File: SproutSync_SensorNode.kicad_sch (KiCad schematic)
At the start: 0 parts

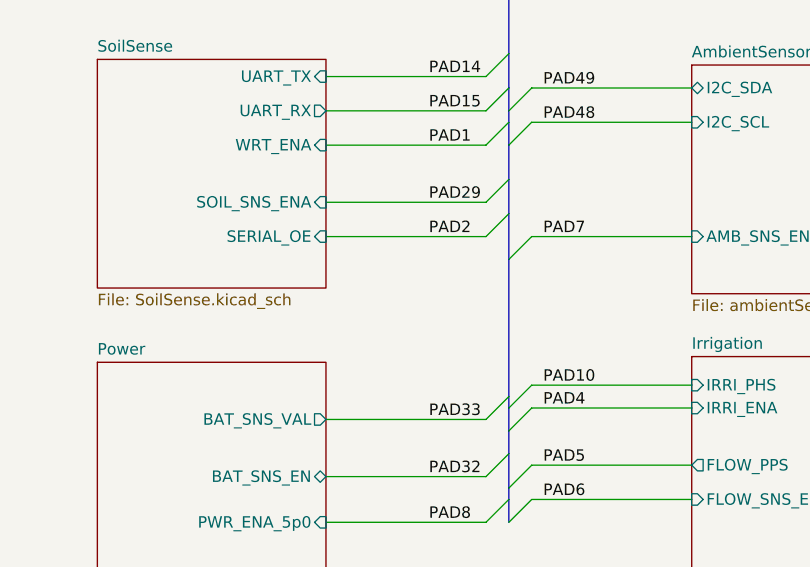
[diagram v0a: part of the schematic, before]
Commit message: replaced soil_sns frontend with SN74
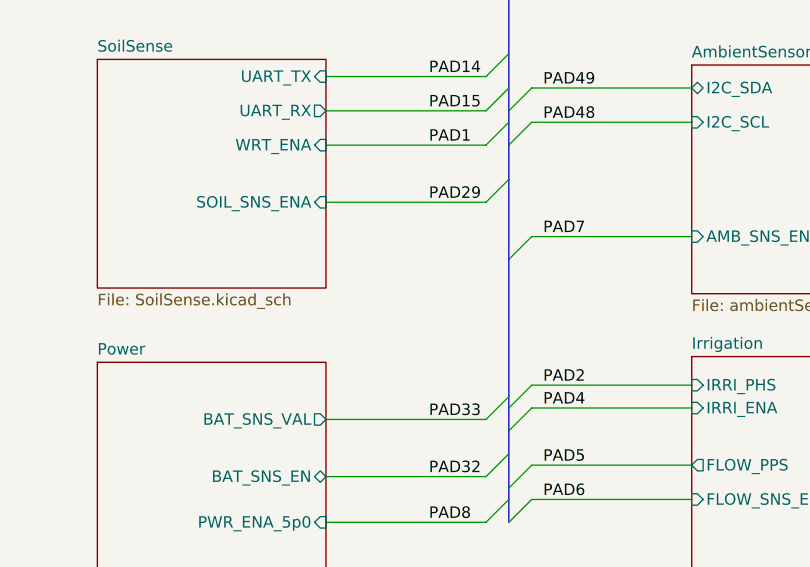
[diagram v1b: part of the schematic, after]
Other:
- sheet SoilSense ports: added none; removed SERIAL_OE
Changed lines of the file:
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@@
-	)
-	(bus_entry
-		(at 128.27 95.25)
-		(size 2.54 -2.54)
-		(stroke
-			(width 0)
-			(type default)
-		)
 	)
 	(bus_entry
@@
 		)
 	)
-	(bus
-		(pts
-			(xy 130.81 88.9) (xy 130.81 92.71)
-		)
-		(stroke
-			(width 0)
-			(type default)
-		)
-	)
 	(wire
 		(pts
@@
 	(wire
 		(pts
-			(xy 110.49 95.25) (xy 128.27 95.25)
-		)
-		(stroke
-			(width 0)
-			(type default)
-		)
-	)
-	(wire
-		(pts
 			(xy 144.78 34.29) (xy 144.78 49.53)
 		)
@@
 	(bus
 		(pts
-			(xy 130.81 92.71) (xy 130.81 97.79)
+			(xy 130.81 88.9) (xy 130.81 97.79)
 		)
 		(stroke
@@
 		)
 	)
-	(label "PAD10"
+	(label "PAD2"
 		(at 134.62 111.76 0)
-		(effects
-			(font
-				(size 1.27 1.27)
-			)
-			(justify left bottom)
-		)
-	)
-	(label "PAD2"
-		(at 121.92 95.25 0)
 		(effects
 			(font
@@
 			)
 		)
-		(pin "SERIAL_OE" input
-			(at 110.49 95.25 0)
-			(effects
-				(font
-					(size 1.27 1.27)
-				)
-				(justify right)
-			)
-		)

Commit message: updated schematic for pwr savings
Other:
- title: SproutSyncProto-A-01 -> SproutSyncProto-A-02
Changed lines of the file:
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@@
 (kicad_sch
-	(version 20250114)
+	(version 20260306)
 	(generator "eeschema")
-	(generator_version "9.0")
+	(generator_version "10.0")
 	(paper "A4")
 	(title_block
-		(title "SproutSyncProto-A-01")
-		(date "2025-07-16")
-		(rev "0.1")
+		(title "SproutSyncProto-A-02")
+		(date "2026-04-29")
+		(rev "0.2")
 		(company "SproutSync LTD")
 		(comment 1 "ALL RIGHTS RESERVED")
@@
 		)
 		(fill
-			(color 0 0 0 0.0000)
+			(color 0 0 0 0)
 		)
 		(property "Sheetname" "PetalStackingConectors"
 			(at 85.09 19.6084 0)
+			(show_name no)
+			(do_not_autoplace no)
 			(effects
 				(font
@@
 		(property "Sheetfile" "SensorNode_PetalStackingConnectors.kicad_sch"
 			(at 71.374 52.578 0)
+			(show_name no)
+			(do_not_autoplace no)
 			(effects
 				(font
@@
 		)
 		(fill
-			(color 0 0 0 0.0000)
+			(color 0 0 0 0)
 		)
 		(property "Sheetname" "AmbientSensors"
 			(at 151.13 75.4884 0)
+			(show_name no)
+			(do_not_autoplace no)
 			(effects
 				(font
@@
 		(property "Sheetfile" "ambientSensors.kicad_sch"
 			(at 151.13 102.1846 0)
+			(show_name no)
+			(do_not_autoplace no)
 			(effects
 				(font
@@
 		)
 		(fill
-			(color 0 0 0 0.0000)
+			(color 0 0 0 0)
 		)
 		(property "Sheetname" "UserPeriphs"
 			(at 151.13 50.7234 0)
+			(show_name no)
+			(do_not_autoplace no)
 			(effects
 				(font
@@
 		(property "Sheetfile" "UserPeriphs.kicad_sch"
 			(at 151.13 66.6246 0)
+			(show_name no)
+			(do_not_autoplace no)
 			(effects
 				(font
@@
 		)
 		(fill
-			(color 0 0 0 0.0000)
+			(color 0 0 0 0)
 		)
 		(property "Sheetname" "Power"
 			(at 85.09 108.5084 0)
+			(show_name no)
+			(do_not_autoplace no)
 			(effects
 				(font
@@
 		(property "Sheetfile" "Power.kicad_sch"
 			(at 85.09 135.2046 0)
+			(show_name no)
+			(do_not_autoplace no)
 			(effects
 				(font
@@
 		)
 		(fill
-			(color 0 0 0 0.0000)
+			(color 0 0 0 0)
 		)
 		(property "Sheetname" "Irrigation"
 			(at 151.13 107.8734 0)
+			(show_name no)
+			(do_not_autoplace no)
 			(effects
 				(font
@@
 		(property "Sheetfile" "Irrigation.kicad_sch"
 			(at 151.13 134.5696 0)
+			(show_name no)
+			(do_not_autoplace no)
 			(effects
 				(font
@@
 		)
 		(fill
-			(color 0 0 0 0.0000)
+			(color 0 0 0 0)
 		)
 		(property "Sheetname" "DebugProbe"
 			(at 151.13 24.0534 0)
+			(show_name no)
+			(do_not_autoplace no)
 			(effects
 				(font
@@
 		(property "Sheetfile" "DebugProbe.kicad_sch"
 			(at 151.13 45.0346 0)
+			(show_name no)
+			(do_not_autoplace no)
 			(effects
 				(font
@@
 		)
 		(fill
-			(color 0 0 0 0.0000)
+			(color 0 0 0 0)
 		)
 		(property "Sheetname" "SoilSense"
 			(at 85.09 74.8534 0)
+			(show_name no)
+			(do_not_autoplace no)
 			(effects
 				(font
@@
 		(property "Sheetfile" "SoilSense.kicad_sch"
 			(at 85.09 101.5496 0)
-			(effects
-				(font
+			(show_name no)
+			(do_not_autoplace no)
+			(effects
+				(font

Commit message: updated pcb for pwr savings
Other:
- title: SproutSyncProto-A-02 -> SproutSyncProto-A-04
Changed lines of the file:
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@@
 	(paper "A4")
 	(title_block
-		(title "SproutSyncProto-A-02")
-		(date "2026-04-29")
+		(title "SproutSyncProto-A-04")
+		(date "2026-05-04")
 		(rev "0.2")
 		(company "SproutSync LTD")
